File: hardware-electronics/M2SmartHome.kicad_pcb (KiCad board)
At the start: 4 copper layers, 22 x 76 mm, 208 parts, among them J1 M.2-Key-M-edge-connector, J3 CONMHF1-SMD-T, J4 CONMHF1-SMD-T, J5 Micro_SD_Card_Det_Hirose_DM3AT, U1 RTL8188FTV-VC-CG, U10 24AA04T-I_OT, U2 EMMC16G-MW28-01E10, U3 PI7C9X440SLBFDE, U4 24AA04T-I_OT, U5 CP2102N-A02-GQFN20, U6 24AA04T-I_OT, U7 EFR32MG21B020F1024IM32-B, U8 USB2244-AEZG-06, U9 USB2244-AEZG-06, Y1 ABM8-12.000MHZ-B2-T, Y2 ECS-240-10-47-CKM-TR, Y3 ECS-240-10-47-CKM-TR, Y4 ABM8-38.400MHZ-10-D1G-T, Y5 ABM8-40.000MHZ-B2-T

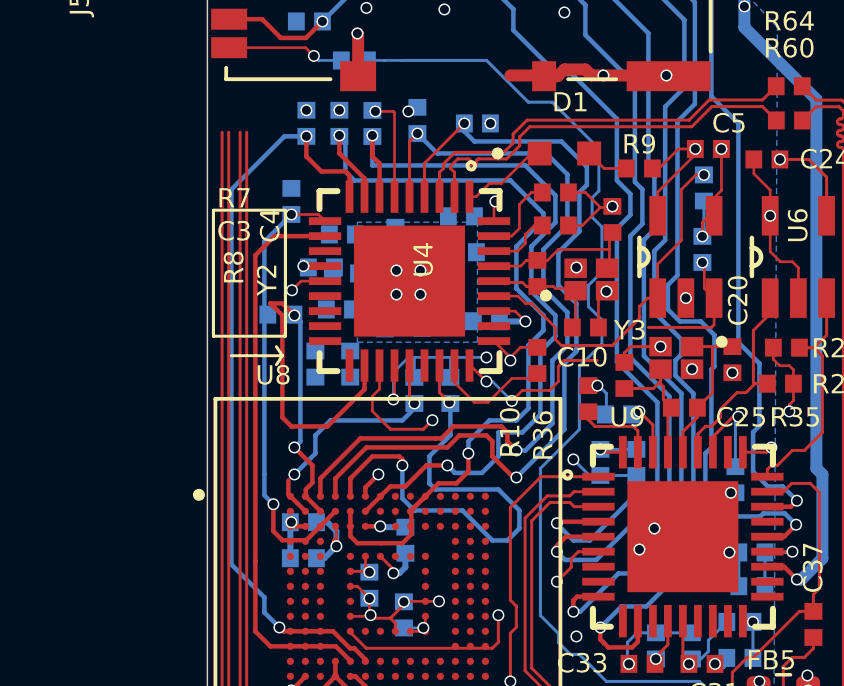
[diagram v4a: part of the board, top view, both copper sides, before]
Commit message: [#17] eMMC routing WIP removed unecessary cap
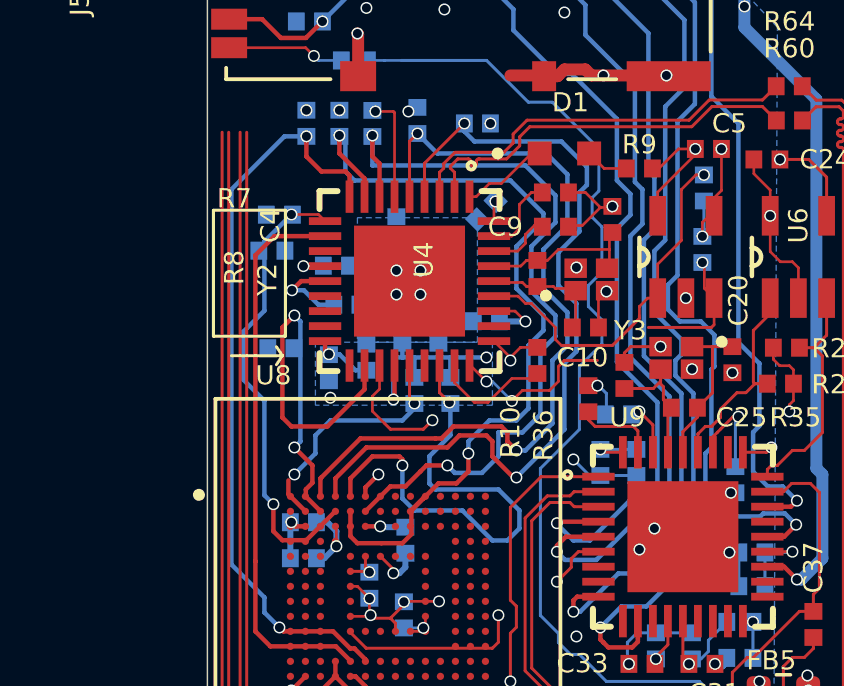
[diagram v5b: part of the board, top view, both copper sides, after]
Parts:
- removed C3, C6: C_100n_0402, M2SmartHomeFootprints:C_0402
- C9: moved to F.Cu
- moved C9 3.18 mm to (92.6, 121.2), turned to 180 degrees
- moved R20 2.41 mm to (83.2, 122.0), turned to 180 degrees
- moved R15 1.12 mm to (83.5, 125.2)
- moved C14 0.86 mm to (90.3, 120.6), turned to 45 degrees
- moved C17 0.76 mm to (87.5, 124.6)
- moved C11 0.73 mm to (88.7, 124.6)
- moved R16 0.60 mm to (83.4, 120.8), turned to 180 degrees
- moved C12 0.59 mm to (86.3, 125.5), turned to -90 degrees
- moved R2 0.47 mm to (85.0, 125.8)
- moved C7 0.40 mm to (85.3, 122.5)
- moved C8 0.35 mm to (87.3, 121.2)
- moved C13 0.30 mm to (85.7, 123.8)
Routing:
- net +3V3_eMMC: track 25.5 -> 28.3 mm, vias 19 -> 20
- net /emmc/~{reset}: track 0.00 -> 1.96 mm, vias 0 -> 1
- net Net-(U2-DAT4): track 16.3 -> 15.0 mm
- net Net-(U8-VDD18): track 0.72 -> 1.39 mm
- net Net-(U2-DAT5): track 14.9 -> 15.4 mm
- added copper zone on B.Cu, net +3V3_eMMC

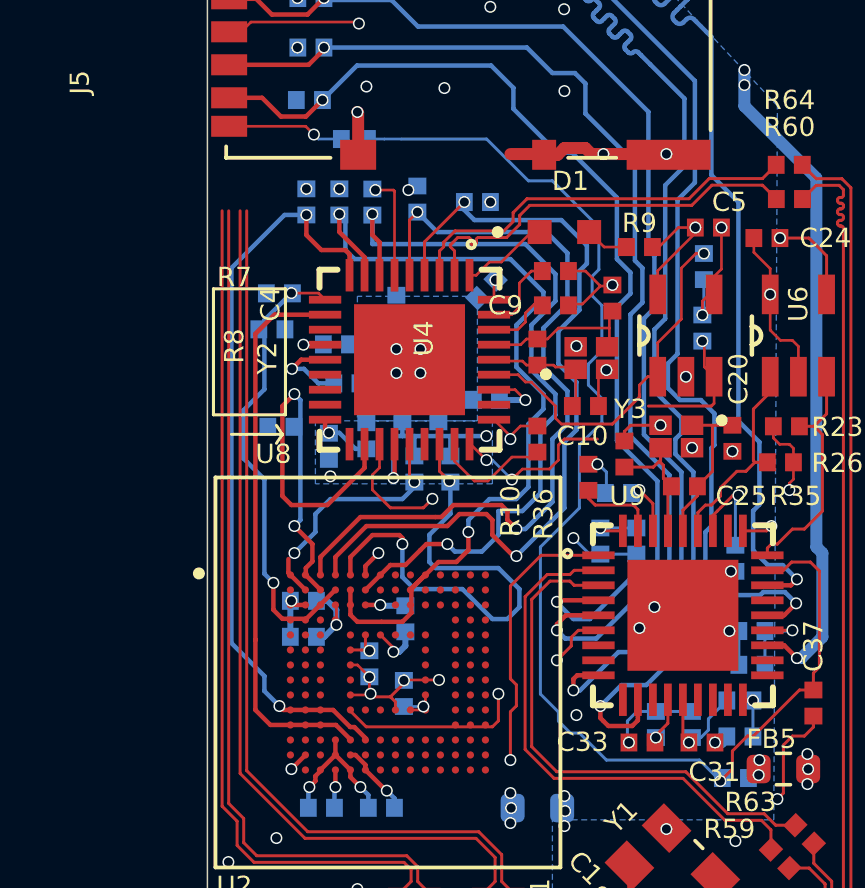
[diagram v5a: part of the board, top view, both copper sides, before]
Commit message: [#17] eMMC routing WIP
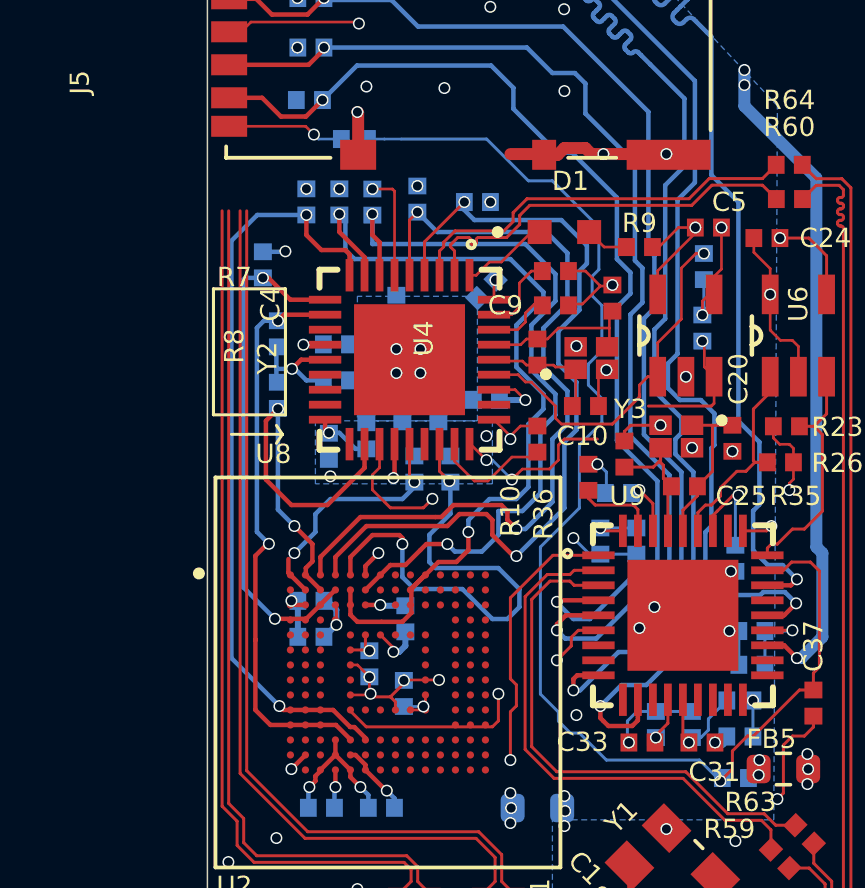
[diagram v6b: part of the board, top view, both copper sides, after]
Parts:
- moved R16 1.10 mm to (82.8, 119.8), turned to 90 degrees
- moved R15 1.05 mm to (83.3, 124.2), turned to 90 degrees
- moved C13 0.36 mm to (85.3, 123.7)
- moved C21 0.25 mm to (84.5, 132.2)
- moved C22 0.25 mm to (84.5, 131.0)
- moved R20 0.25 mm to (83.3, 122.1), turned to -90 degrees
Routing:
- net +3V3_eMMC: track 28.3 -> 26.1 mm, vias 20 -> 21
- net Net-(U2-DAT5): track 15.4 -> 17.2 mm
- net Net-(U2-DAT4): track 15.0 -> 14.3 mm
- net Net-(U2-CLK): track 24.9 -> 25.5 mm
- net GND: track 165.2 -> 164.7 mm
- net Net-(U2-CMD): track 18.7 -> 19.2 mm, vias 0 -> 2

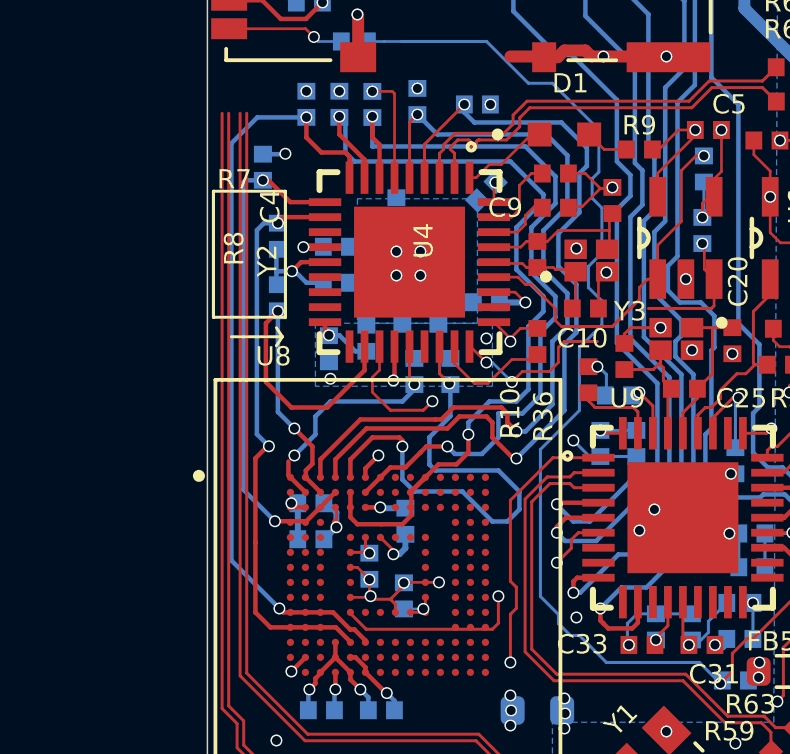
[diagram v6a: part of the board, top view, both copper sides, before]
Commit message: [#17] eMMC routing WIP
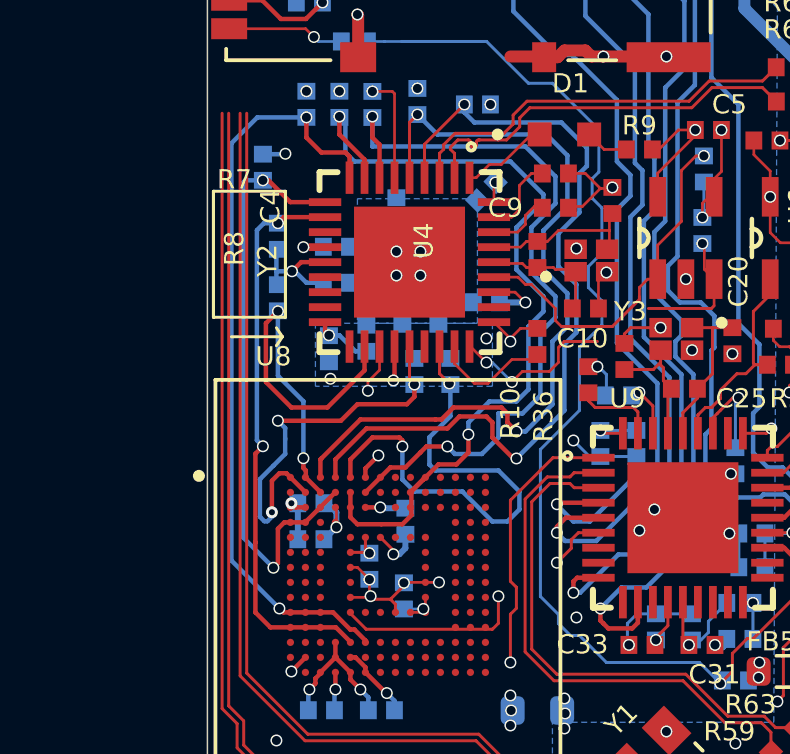
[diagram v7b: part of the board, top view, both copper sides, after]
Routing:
- net +3V3_eMMC: track 26.1 -> 33.9 mm
- net Net-(U2-DAT3): track 8.02 -> 13.5 mm, vias 2 -> 3
- net Net-(U2-DAT5): track 17.2 -> 20.1 mm
- net Net-(U2-RST_N): track 10.2 -> 7.91 mm
